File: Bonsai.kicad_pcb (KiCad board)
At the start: 2 copper layers, 348.5 x 165.6 mm, 202 parts, among them J1 AVR-ISP-6, U1 ATmega32A-PU, Y1 Crystal

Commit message: Fixed missing VCC trace
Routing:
- net VCC: track 12.6 -> 18.4 mm

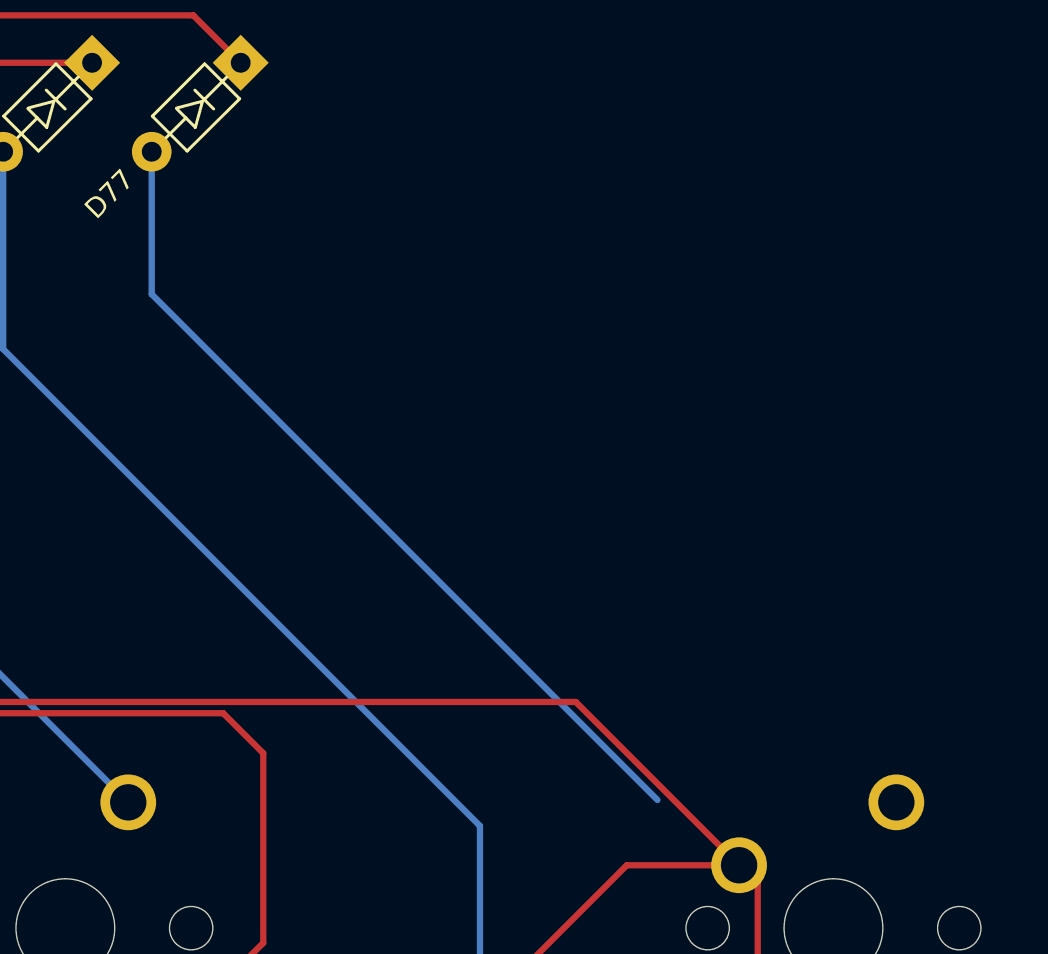
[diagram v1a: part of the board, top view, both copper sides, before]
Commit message: Fixed a missing trace.
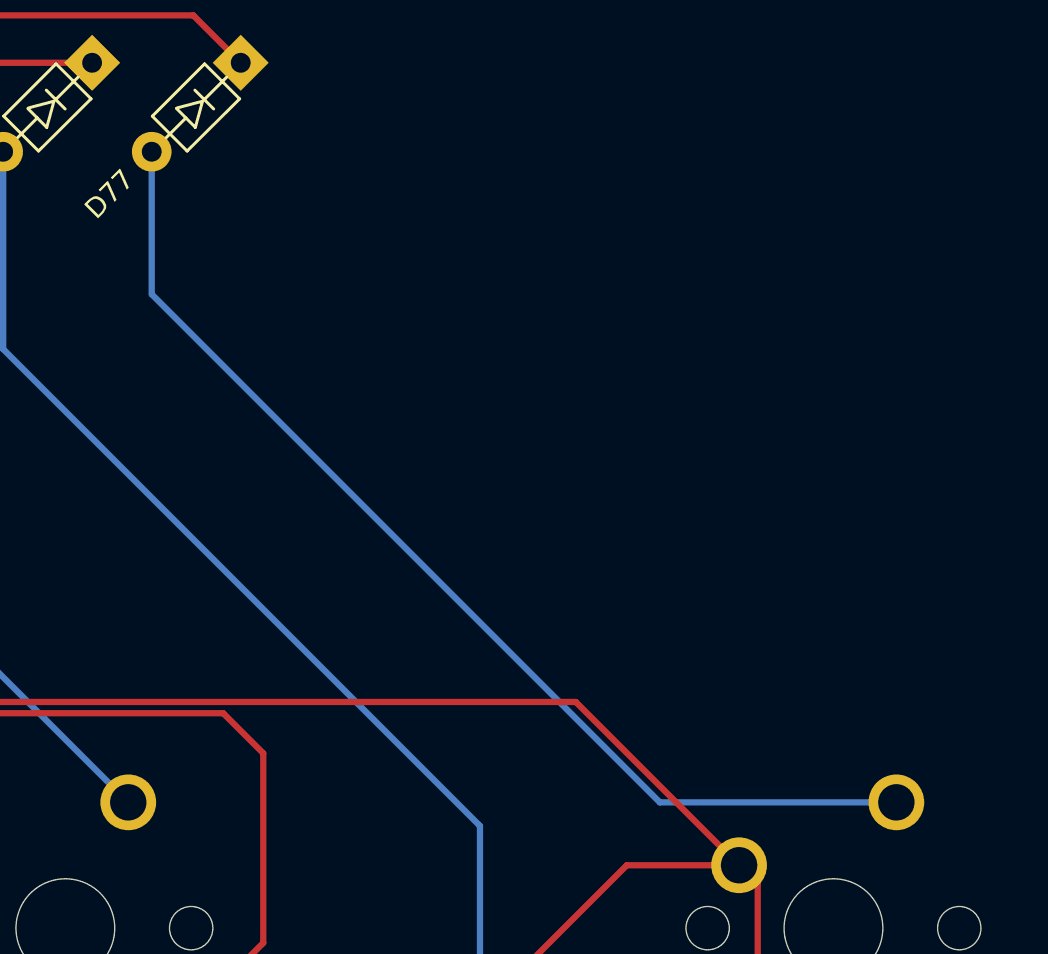
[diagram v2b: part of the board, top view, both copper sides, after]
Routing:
- net Net-(D77-Pad2): track 34.6 -> 44.3 mm

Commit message: Fixed some via too close errors
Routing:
- net row0: track 321.4 -> 323.0 mm
- net row5: track 165.4 -> 166.2 mm
- net row4: track 231.4 -> 232.1 mm
